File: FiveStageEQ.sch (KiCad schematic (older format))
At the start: 75 parts, among them J1 AudioJack3, J2 AudioJack3, U1 LM833, U2 LM833, U3 LM833, U4 LM833, U5 LM833, U6 LM833, U7 LM833, U8 LM317_TO3

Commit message: Added graphics separating stages
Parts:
- C1: symbol Device:CP1_Small -> FiveStageEQ-rescue:CP1_Small-Device
- C10, C11, C12, C13, C14, C15, C16, C17, C18, C19, C2, C20, C21, C22, C23, C24, C25, C26, C27, C28, C29, C3, C4, C5, C6, C7, C8, C9: symbol Device:C_Small -> FiveStageEQ-rescue:C_Small-Device
- J1, J2: symbol Connector:AudioJack3 -> FiveStageEQ-rescue:AudioJack3-Connector
- R1, R10, R11, R12, R13, R14, R15, R16, R17, R18, R19, R2, R20, R21, R22, R23, R24, R25, R26, R27, R3, R33, R34, R35, R36, R4, R5, R6, R7, R8, R9: symbol Device:R_Small_US -> FiveStageEQ-rescue:R_Small_US-Device
- R28, R29, R30, R31, R32: symbol Device:R_Variable_US -> FiveStageEQ-rescue:R_Variable_US-Device
- U8: symbol Regulator_Linear:LM317_TO3 -> FiveStageEQ-rescue:LM317_TO3-Regulator_Linear
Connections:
- net GND: now also J1.S, J2.S; no longer J1.1 (S), J2.1 (S)
- net at C2.2: now also J1.T; no longer J1.2 (T)
- new net: C28.1, J2.R, J2.T

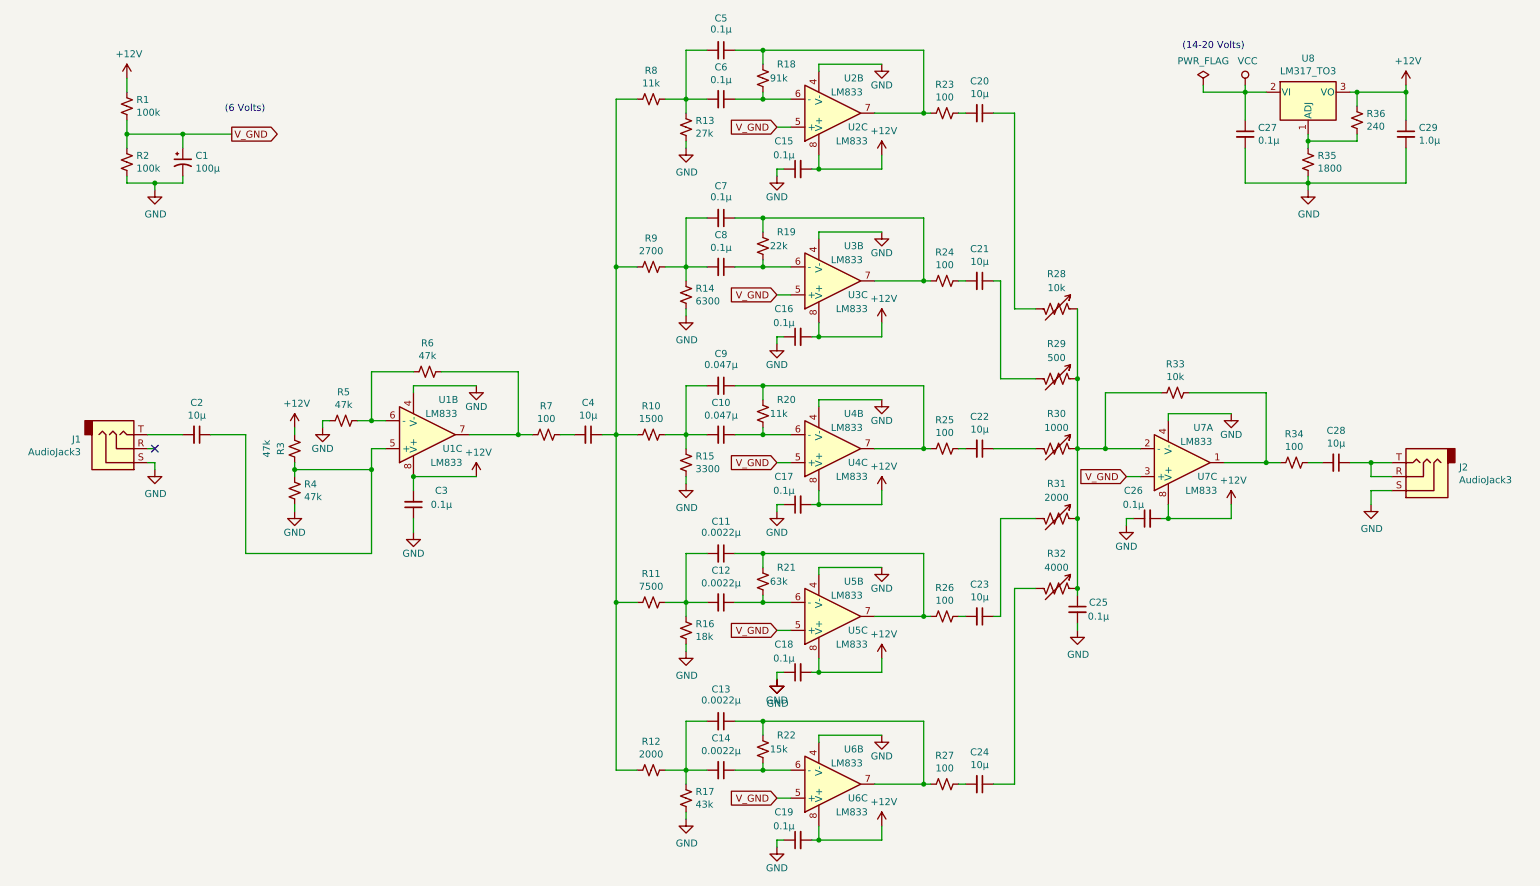
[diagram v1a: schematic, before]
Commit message: added poster of EQ
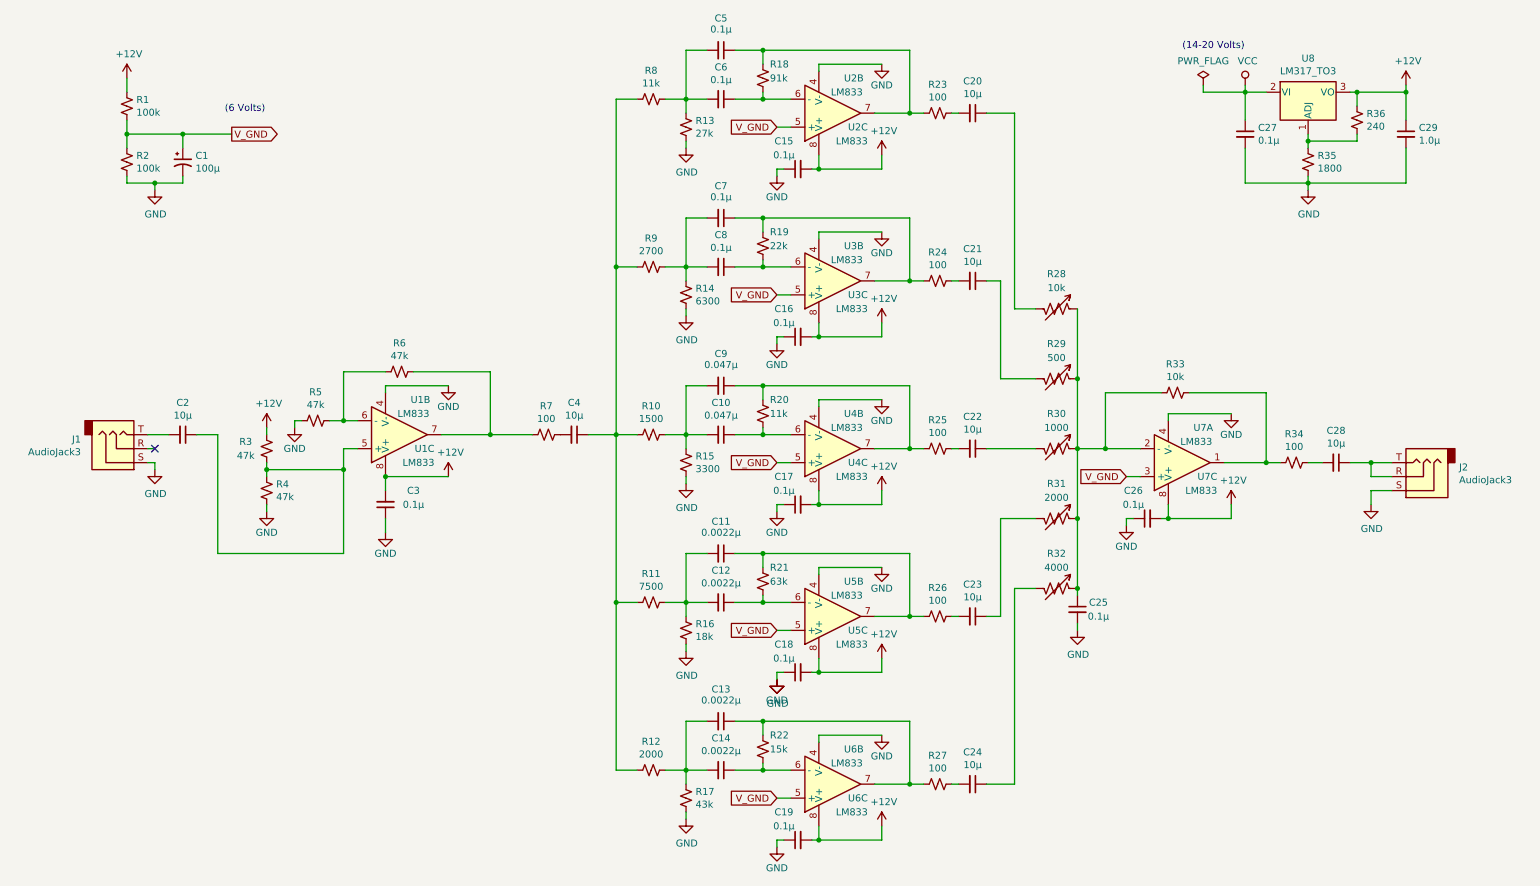
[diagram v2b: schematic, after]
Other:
- moved on the sheet: C2, C20, C21, C22, C23, C24, C3, C4, R23, R24, R25, R26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
